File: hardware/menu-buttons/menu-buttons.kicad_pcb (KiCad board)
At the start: 2 copper layers, 29.2 x 40.6 mm, 8 parts, among them J1 Conn_01x05, SW1 Menu, SW2 Set, SW3 Up, SW4 Down

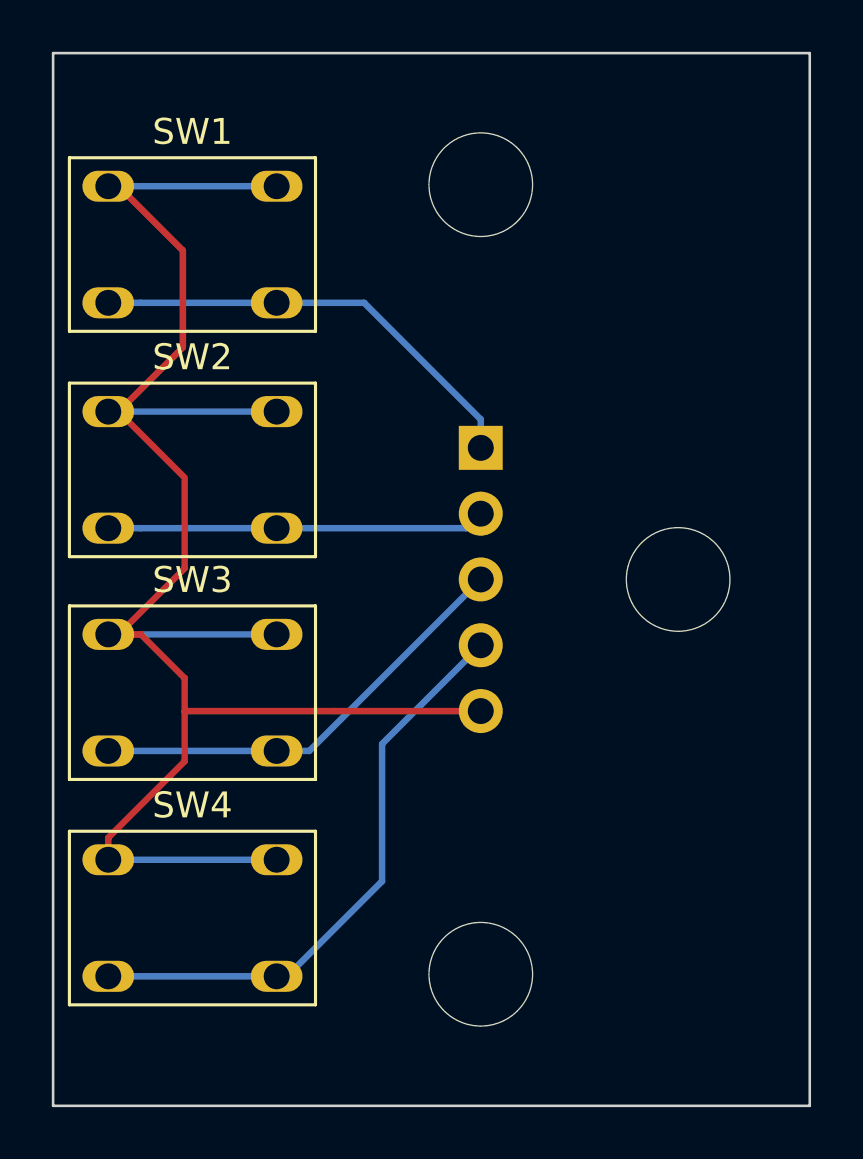
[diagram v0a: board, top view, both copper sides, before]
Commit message: Update menu buttons PCB
Smaller mounting holes, correct Molex header
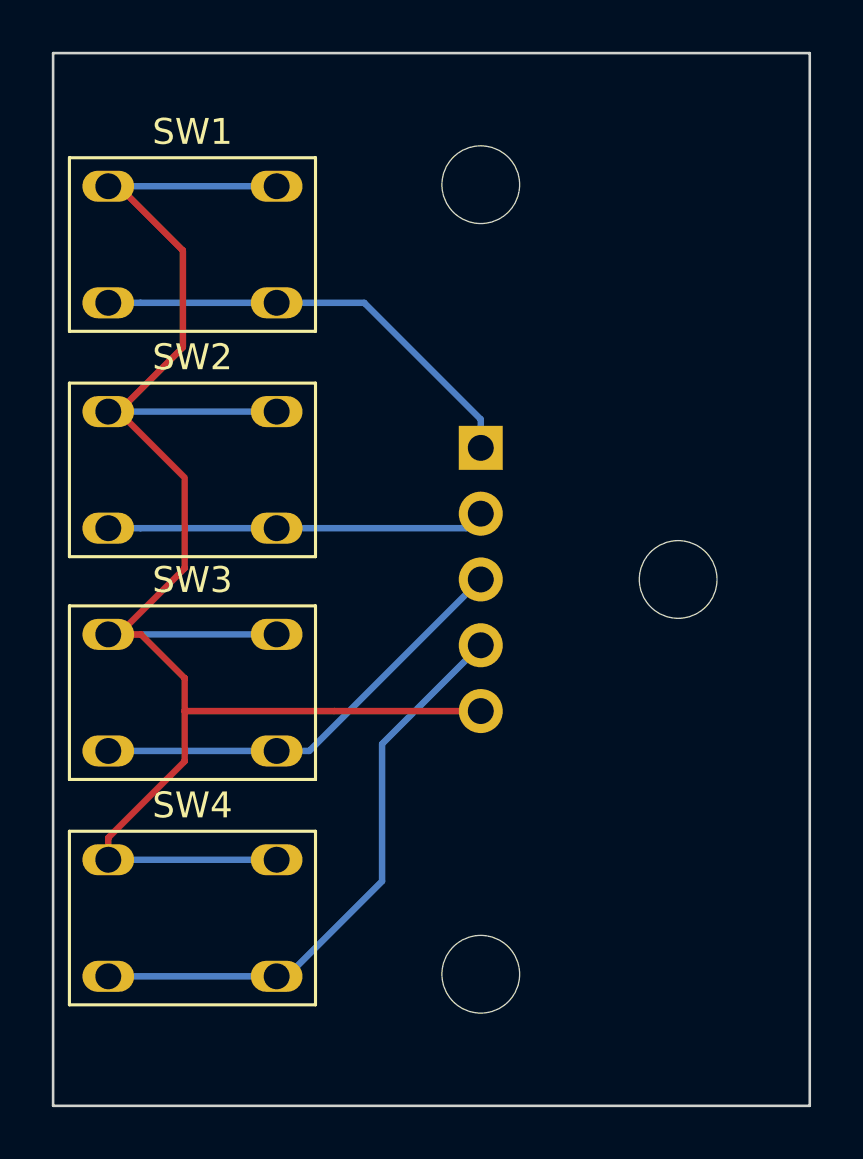
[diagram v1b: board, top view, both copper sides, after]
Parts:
- J1: footprint Connector_PinHeader_2.54mm:PinHeader_1x05_P2.54mm_Vertical -> Connector_PinHeader_2.54mm:Molex_KK254_1x05Vertical
- REF** (x3): value MountingHole_4mm -> MountingHole_3mm; footprint MountingHole:MountingHole_4mm -> MountingHole:MountingHole_3mm

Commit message: Menu buttons PCB update
Update to Rev A PCB as ordered
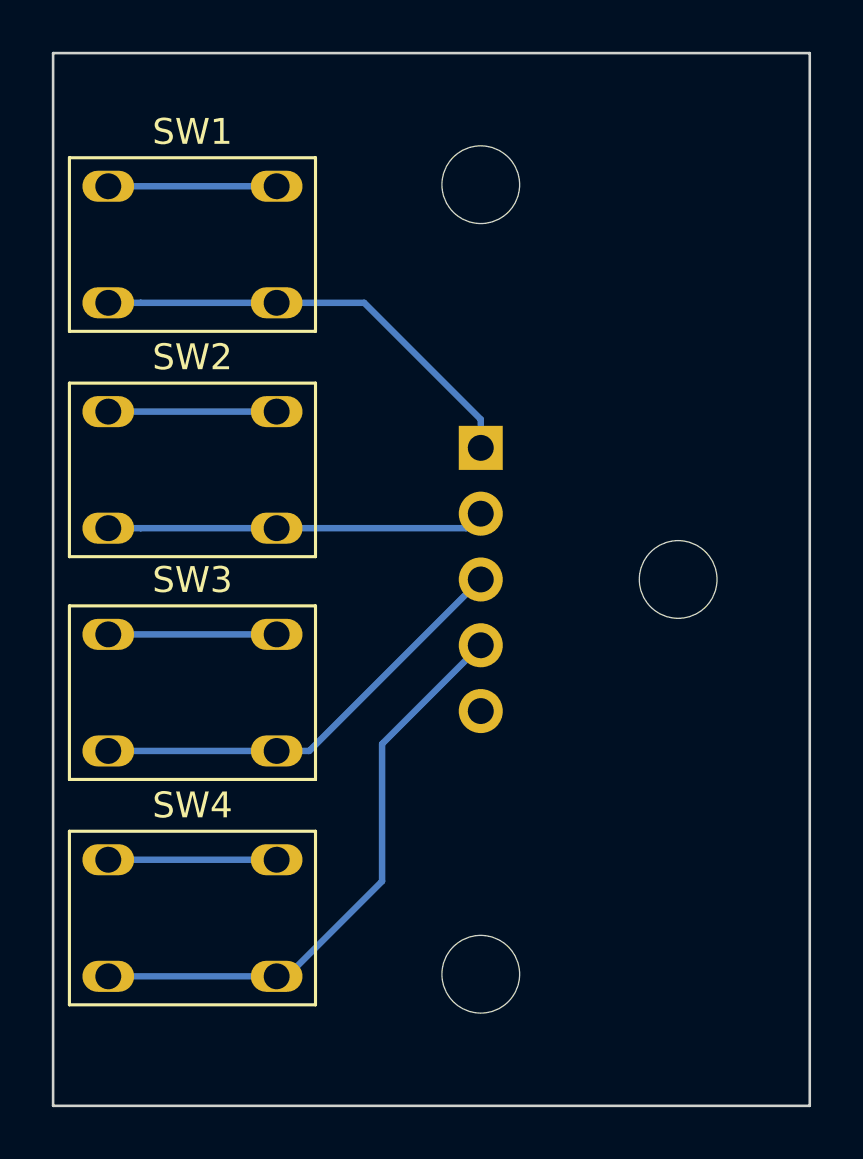
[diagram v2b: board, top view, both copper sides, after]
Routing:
- net Net-(J1-Pad5): track 71.9 -> 27.2 mm
- added copper zone on B.Cu, net Net-(J1-Pad5)
- added copper zone on F.Cu, net Net-(J1-Pad5)
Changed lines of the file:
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@@
     (thickness 1.6)
     (drawings 5)
-    (tracks 37)
+    (tracks 24)
     (zones 0)
     (modules 8)
@@
   (segment (start 143.25 77.05) (end 136.75 77.05) (width 0.25) (layer B.Cu) (net 5))
   (segment (start 143.25 85.75) (end 136.75 85.75) (width 0.25) (layer B.Cu) (net 5))
-  (segment (start 137.15 59.75) (end 139.63 62.23) (width 0.25) (layer F.Cu) (net 5))
   (segment (start 136.75 59.75) (end 137.15 59.75) (width 0.25) (layer F.Cu) (net 5))
-  (segment (start 139.63 62.23) (end 139.63 65.97) (width 0.25) (layer F.Cu) (net 5))
   (segment (start 137.15 68.45) (end 136.75 68.45) (width 0.25) (layer F.Cu) (net 5))
-  (segment (start 139.63 65.97) (end 137.15 68.45) (width 0.25) (layer F.Cu) (net 5))
-  (segment (start 137.15 68.45) (end 139.7 71) (width 0.25) (layer F.Cu) (net 5))
-  (segment (start 137.15 77.05) (end 139.7 74.5) (width 0.25) (layer F.Cu) (net 5))
   (segment (start 136.75 77.05) (end 137.15 77.05) (width 0.25) (layer F.Cu) (net 5))
-  (segment (start 139.7 74.5) (end 139.7 71.12) (width 0.25) (layer F.Cu) (net 5))
-  (segment (start 145.47 80.01) (end 139.7 80.01) (width 0.25) (layer F.Cu) (net 5))
-  (segment (start 136.75 77.05) (end 138.01 77.05) (width 0.25) (layer F.Cu) (net 5))
-  (segment (start 138.01 77.05) (end 139.7 78.74) (width 0.25) (layer F.Cu) (net 5))
-  (segment (start 136.75 84.9) (end 136.75 85.75) (width 0.25) (layer F.Cu) (net 5))
-  (segment (start 139.7 81.95) (end 136.75 84.9) (width 0.25) (layer F.Cu) (net 5))
-  (segment (start 139.7 78.74) (end 139.7 81.95) (width 0.25) (layer F.Cu) (net 5))
-  (segment (start 145.47 80.01) (end 151.13 80.01) (width 0.25) (layer F.Cu) (net 5))
+  (zone (net 5) (net_name "Net-(J1-Pad5)") (layer F.Cu) (hatch edge 0.508)
+    (connect_pads (clearance 0.508))
+    (min_thickness 0.254)
+    (fill yes (arc_segments 32) (thermal_gap 0.508) (thermal_bridge_width 0.508))
+    (polygon
+      (pts
+        (xy 134.62 54.61) (xy 163.83 54.61) (xy 163.83 95.25) (xy 134.62 95.25)
+      )
+    )
+  )
+  (zone (net 5) (net_name "Net-(J1-Pad5)") (layer B.Cu) (hatch edge 0.508)
+    (connect_pads (clearance 0.508))
+    (min_thickness 0.254)
+    (fill yes (arc_segments 32) (thermal_gap 0.508) (thermal_bridge_width 0.508))
+    (polygon
+      (pts
+        (xy 134.62 54.61) (xy 163.83 54.61) (xy 163.83 95.25) (xy 134.62 95.25)
+      )
+    )
+  )
 )

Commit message: PCB updates
Correction to motherboard R value, update of buttons PCB to rev B as ordered to go in case with reduced clearance
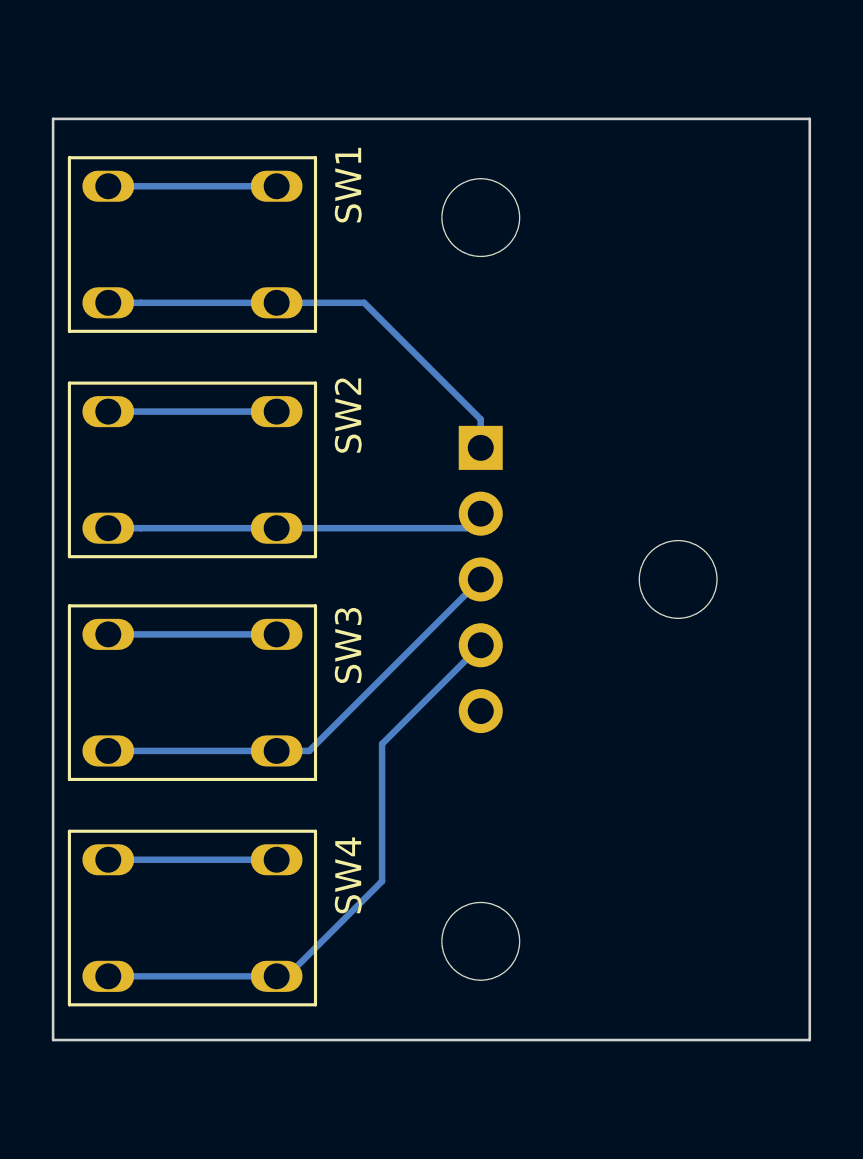
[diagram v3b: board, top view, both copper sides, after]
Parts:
- moved REF** 1.27 mm to (151.1, 61.0)
- moved REF** 1.27 mm to (151.1, 88.9)
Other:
- board size 29.2 x 40.6 mm -> 29.2 x 35.6 mm
- board text added: "ADC Theatre Bar Lighting Controller Menu Buttons Rev B"
- board text removed: "ADC Theatre Bar Lighting Controller Menu Buttons Rev A"
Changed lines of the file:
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@@
       (drillshape 0)
       (scaleselection 1)
-      (outputdirectory "/Users/John/Desktop/"))
+      (outputdirectory "/Users/John/Desktop/buttonsgerber2/"))
   )
   (net 0 "")
@@
   )
   (module MountingHole:MountingHole_3mm (layer F.Cu)
-    (at 151.13 90.17)
+    (at 151.13 88.9)
     (descr "Mounting Hole 3mm, no annular")
     (tags "mounting hole 3mm no annular")
@@
   )
   (module MountingHole:MountingHole_3mm (layer F.Cu)
-    (at 151.13 59.69)
+    (at 151.13 60.96)
     (descr "Mounting Hole 3mm, no annular")
     (tags "mounting hole 3mm no annular")
@@
   (module Button_Switch_THT:TE6mmTactSW (layer F.Cu)
     (at 140 62 270)
-    (fp_text reference SW1 (at -4.35 0) (layer F.SilkS)
+    (fp_text reference SW1 (at -2.31 -6.05 90) (layer F.SilkS)
       (effects (font (size 1 1) (thickness 0.15)))
     )
@@
   (module Button_Switch_THT:TE6mmTactSW (layer F.Cu)
     (at 140 70.7 270)
-    (fp_text reference SW2 (at -4.35 0) (layer F.SilkS)
+    (fp_text reference SW2 (at -2.12 -6.05 90) (layer F.SilkS)
       (effects (font (size 1 1) (thickness 0.15)))
     )
@@
   (module Button_Switch_THT:TE6mmTactSW (layer F.Cu)
     (at 140 79.3 270)
-    (fp_text reference SW3 (at -4.35 0) (layer F.SilkS)
+    (fp_text reference SW3 (at -1.83 -6.05 90) (layer F.SilkS)
       (effects (font (size 1 1) (thickness 0.15)))
     )
@@
   (module Button_Switch_THT:TE6mmTactSW (layer F.Cu)
     (at 140 88 270)
-    (fp_text reference SW4 (at -4.35 0) (layer F.SilkS)
+    (fp_text reference SW4 (at -1.64 -6.05 90) (layer F.SilkS)
       (effects (font (size 1 1) (thickness 0.15)))
     )
@@
       (net 5 "Net-(J1-Pad5)"))
   )
-  (gr_text "ADC Theatre Bar \nLighting Controller\nMenu Buttons Rev A\n" (at 161 94.5 -90) (layer B.SilkS)
+  (gr_text "ADC Theatre Bar \nLighting Controller\nMenu Buttons \nRev B\n" (at 160.02 92.456 -90) (layer B.SilkS)
     (effects (font (size 1 1) (thickness 0.15)) (justify left mirror))
   )
-  (gr_line (start 134.62 95.25) (end 134.62 54.61) (layer Edge.Cuts) (width 0.1))
-  (gr_line (start 163.83 95.25) (end 134.62 95.25) (layer Edge.Cuts) (width 0.1))
-  (gr_line (start 163.83 54.61) (end 163.83 95.25) (layer Edge.Cuts) (width 0.1))
-  (gr_line (start 134.62 54.61) (end 163.83 54.61) (layer Edge.Cuts) (width 0.1))
+  (gr_line (start 134.62 92.71) (end 134.62 57.15) (layer Edge.Cuts) (width 0.1))
+  (gr_line (start 163.83 92.71) (end 134.62 92.71) (layer Edge.Cuts) (width 0.1))
+  (gr_line (start 163.83 57.15) (end 163.83 92.71) (layer Edge.Cuts) (width 0.1))
+  (gr_line (start 134.62 57.15) (end 163.83 57.15) (layer Edge.Cuts) (width 0.1))
   (segment (start 138 64.25) (end 143.25 64.25) (width 0.25) (layer B.Cu) (net 1))
   (segment (start 136.75 64.25) (end 138 64.25) (width 0.25) (layer B.Cu) (net 1))
@@
     (polygon
       (pts
-        (xy 134.62 54.61) (xy 163.83 54.61) (xy 163.83 95.25) (xy 134.62 95.25)
+        (xy 134.62 57.15) (xy 163.83 57.15) (xy 163.83 92.71) (xy 134.62 92.71)
       )
     )
@@
     (polygon
       (pts
-        (xy 134.62 54.61) (xy 163.83 54.61) (xy 163.83 95.25) (xy 134.62 95.25)
+        (xy 134.62 57.15) (xy 163.83 57.15) (xy 163.83 92.71) (xy 134.62 92.71)
       )
     )
